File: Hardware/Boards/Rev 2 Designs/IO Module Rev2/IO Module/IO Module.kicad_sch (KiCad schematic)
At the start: 0 parts

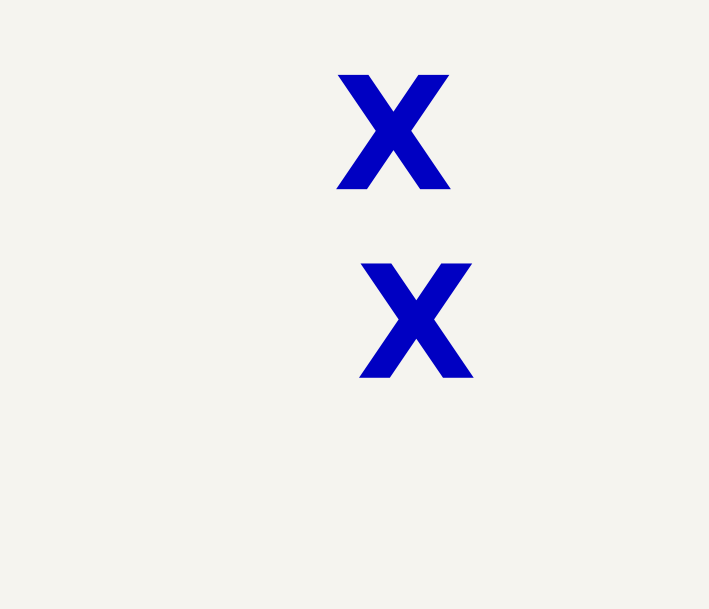
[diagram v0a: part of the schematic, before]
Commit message: Rev 2 IO module complete
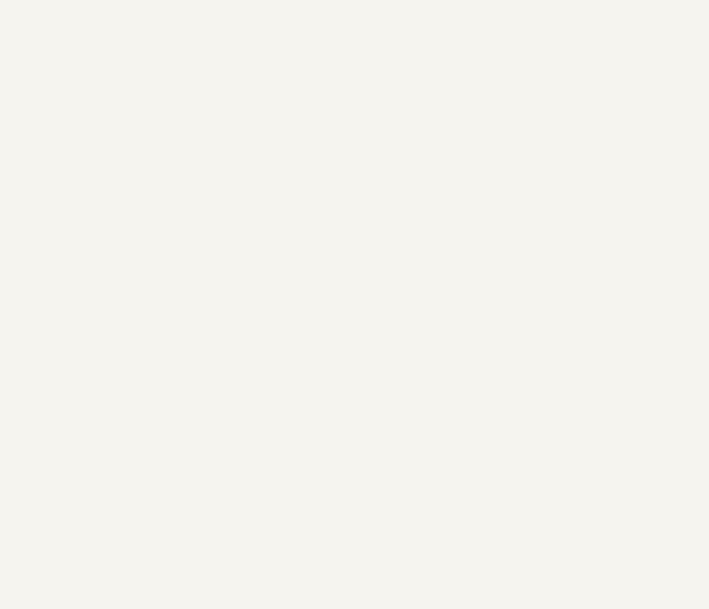
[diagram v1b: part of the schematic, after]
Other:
- note removed: "X"
